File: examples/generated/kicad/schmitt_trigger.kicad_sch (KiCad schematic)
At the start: 6 parts

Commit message: Attempt to create legible symbols.
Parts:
- R1, R2, R3: symbol examples:R -> R
- VCC, VIN: symbol examples:VSOURCE -> VSOURCE
- XU1: symbol examples:OPAMP -> OPAMP
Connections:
- net GND: now also R1.1, VCC.1 (E1), VCC.2 (E2), VIN.2 (E2)
- new net: R3.1, VIN.1 (E1)
- new net: R3.2, XU1.1 (+)
- new net: R1.2, R2.1, XU1.3
- new net: R2.2, XU1.2 (-)
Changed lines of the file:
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@@
     (comment 1 "Generated by mixedsig2cad")
   )
-  (symbol (lib_id "examples:VSOURCE") (at 45.00 40.00 0) (unit 1)
+  (symbol (lib_id "VSOURCE") (at 45.00 40.00 0) (unit 1)
     (in_bom yes) (on_board yes)
     (property "Reference" "VCC" (at 45.0 36.19 0)
@@
     )
   )
-  (symbol (lib_id "examples:VSOURCE") (at 45.00 105.00 90) (unit 1)
+  (symbol (lib_id "VSOURCE") (at 45.00 105.00 90) (unit 1)
     (in_bom yes) (on_board yes)
     (property "Reference" "VIN" (at 45.0 101.19 0)
@@
     )
   )
-  (symbol (lib_id "examples:R") (at 95.00 40.00 90) (unit 1)
+  (symbol (lib_id "R") (at 95.00 40.00 90) (unit 1)
     (in_bom yes) (on_board yes)
     (property "Reference" "R1" (at 95.0 36.19 0)
@@
     )
   )
-  (symbol (lib_id "examples:R") (at 140.00 55.00 90) (unit 1)
+  (symbol (lib_id "R") (at 140.00 55.00 90) (unit 1)
     (in_bom yes) (on_board yes)
     (property "Reference" "R2" (at 140.0 51.19 0)
@@
     )
   )
-  (symbol (lib_id "examples:R") (at 95.00 105.00 90) (unit 1)
+  (symbol (lib_id "R") (at 95.00 105.00 90) (unit 1)
     (in_bom yes) (on_board yes)
     (property "Reference" "R3" (at 95.0 101.19 0)
@@
     )
   )
-  (symbol (lib_id "examples:OPAMP") (at 145.00 85.00 0) (unit 1)
+  (symbol (lib_id "OPAMP") (at 145.00 85.00 0) (unit 1)
     (in_bom yes) (on_board yes)
     (property "Reference" "XU1" (at 145.0 81.19 0)
@@
     )
   )
-  (symbol (lib_id "examples:GND") (at 33.00 26.38 0) (unit 1)
+  (symbol (lib_id "GND") (at 33.00 26.38 0) (unit 1)
     (in_bom yes) (on_board yes)
     (property "Reference" "#PWR0001" (at 33.0 22.570000000000004 0)
@@
     )
   )
-  (symbol (lib_id "examples:VCC") (at 33.00 34.00 0) (unit 1)
+  (symbol (lib_id "VCC") (at 33.00 34.00 0) (unit 1)
     (in_bom yes) (on_board yes)
     (property "Reference" "#PWR0002" (at 33.0 30.19 0)

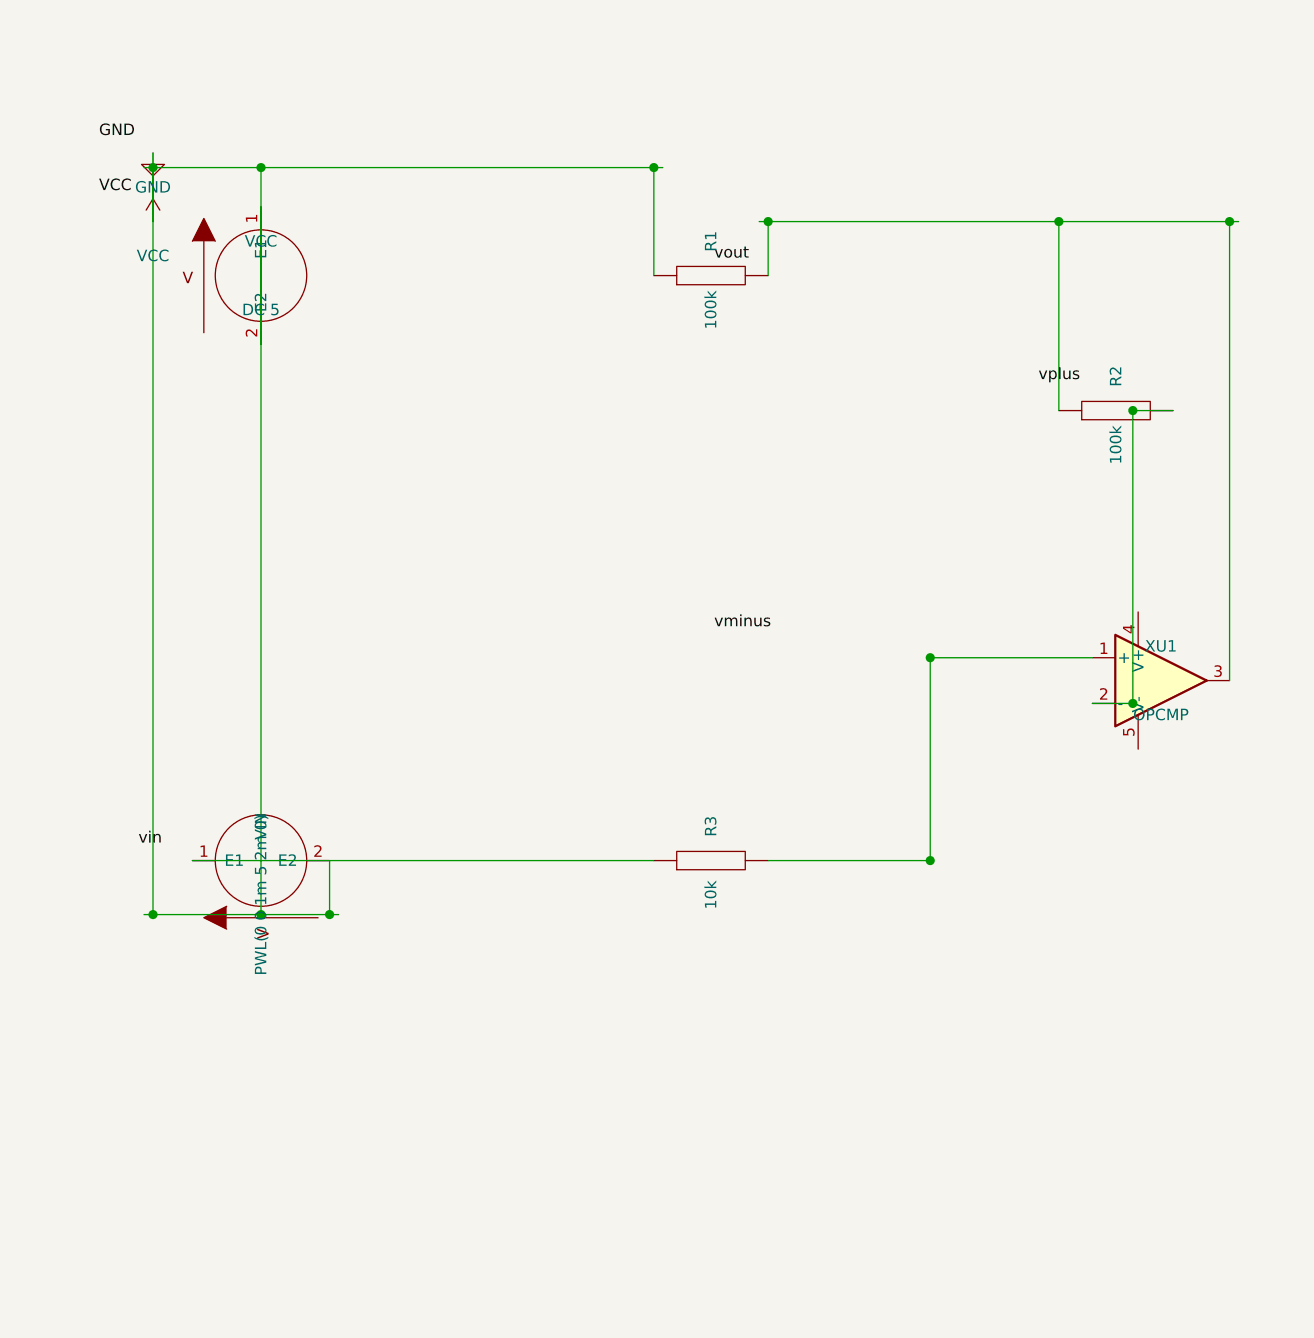
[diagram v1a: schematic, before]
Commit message: Attempt full seperation of circuit concerns into layers.
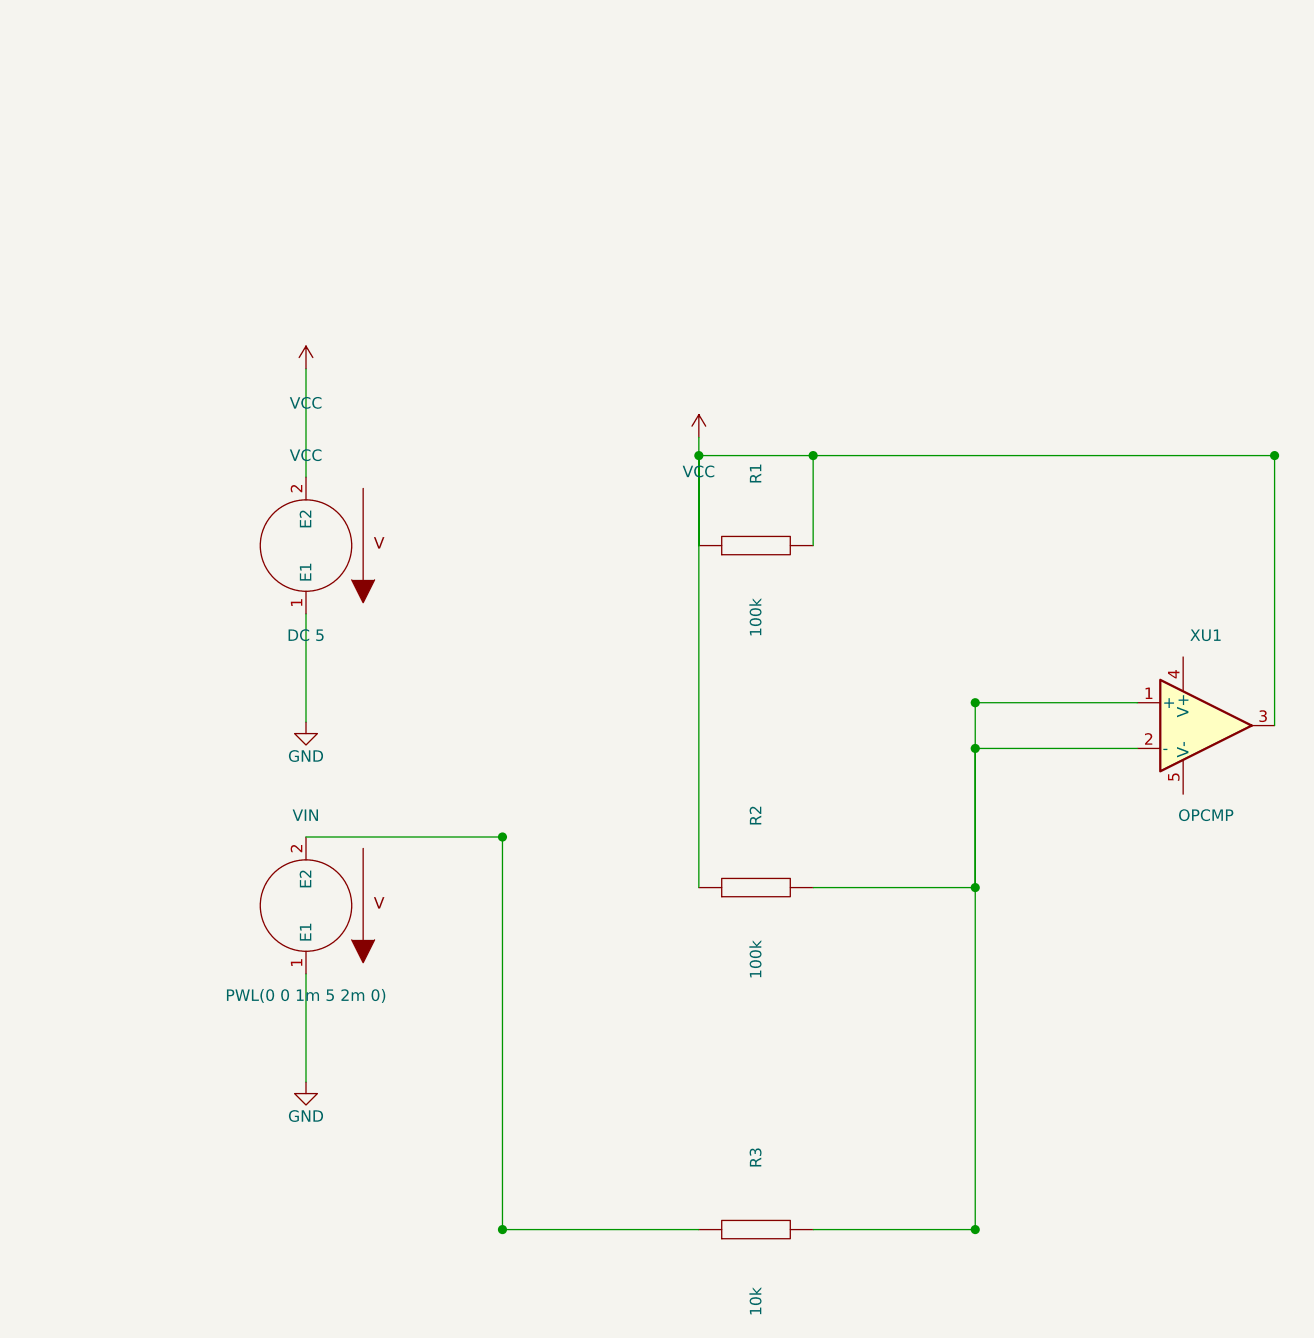
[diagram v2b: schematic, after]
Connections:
- net GND: now also VIN.1 (E1); no longer R1.1, VCC.2 (E2), VIN.2 (E2)
- net at R3.1: now also VIN.2 (E2); no longer VIN.1 (E1)
- net at R3.2, XU1.1 (+): now also R2.2, XU1.2 (-)
- net VCC: now reaches R1.2, R2.1, XU1.3
- net VCC: now also R1.1, VCC.2 (E2)
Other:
- moved on the sheet: R1, R2, R3, VCC, VIN, XU1

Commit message: Add checks for connectivity.
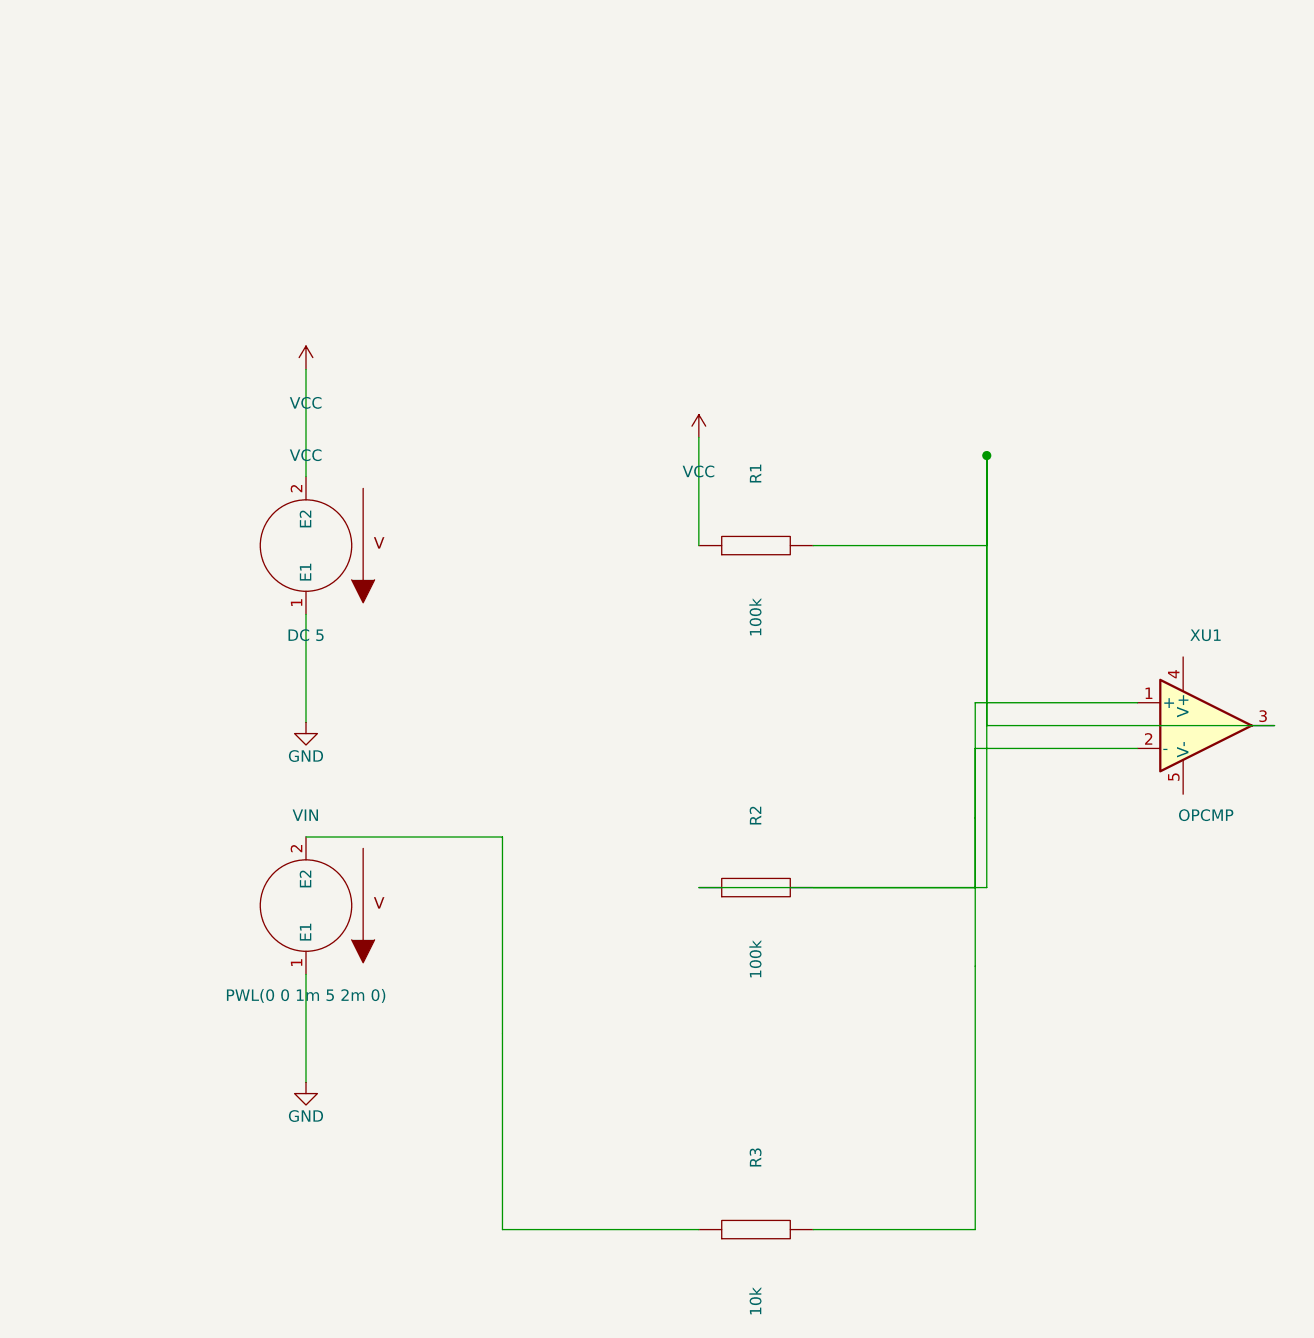
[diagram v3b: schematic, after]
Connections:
- net VCC: no longer R1.2, R2.1, XU1.3
- net at R2.2, R3.2, XU1.1 (+)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: now also R1.2, R2.1, XU1.3
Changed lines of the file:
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@@
     (stroke (width 0) (type solid) (color 0 0 0 0))
   )
-  (wire (pts (xy 71.83 102.38) (xy 71.83 146.00))
+  (wire (pts (xy 71.83 102.38) (xy 71.83 124.19))
     (stroke (width 0) (type solid) (color 0 0 0 0))
   )
-  (wire (pts (xy 71.83 146.00) (xy 93.65 146.00))
+  (wire (pts (xy 93.65 146.00) (xy 71.83 146.00))
+    (stroke (width 0) (type solid) (color 0 0 0 0))
+  )
+  (wire (pts (xy 71.83 146.00) (xy 71.83 124.19))
     (stroke (width 0) (type solid) (color 0 0 0 0))
   )
@@
     (stroke (width 0) (type solid) (color 0 0 0 0))
   )
-  (wire (pts (xy 124.36 146.00) (xy 124.36 87.46))
+  (wire (pts (xy 124.36 146.00) (xy 124.36 116.73))
     (stroke (width 0) (type solid) (color 0 0 0 0))
   )
-  (wire (pts (xy 124.36 87.46) (xy 142.38 87.46))
+  (wire (pts (xy 142.38 87.46) (xy 124.36 87.46))
     (stroke (width 0) (type solid) (color 0 0 0 0))
   )
-  (wire (pts (xy 93.65 60.00) (xy 157.62 60.00))
+  (wire (pts (xy 124.36 87.46) (xy 124.36 116.73))
     (stroke (width 0) (type solid) (color 0 0 0 0))
   )
-  (wire (pts (xy 106.35 70.00) (xy 106.35 60.00))
+  (wire (pts (xy 106.35 70.00) (xy 125.64 70.00))
     (stroke (width 0) (type solid) (color 0 0 0 0))
   )
-  (wire (pts (xy 93.65 108.00) (xy 93.65 60.00))
+  (wire (pts (xy 125.64 70.00) (xy 125.64 60.00))
     (stroke (width 0) (type solid) (color 0 0 0 0))
   )
-  (wire (pts (xy 157.62 90.00) (xy 157.62 60.00))
+  (wire (pts (xy 93.65 108.00) (xy 125.64 108.00))
+    (stroke (width 0) (type solid) (color 0 0 0 0))
+  )
+  (wire (pts (xy 125.64 108.00) (xy 125.64 60.00))
+    (stroke (width 0) (type solid) (color 0 0 0 0))
+  )
+  (wire (pts (xy 157.62 90.00) (xy 125.64 90.00))
+    (stroke (width 0) (type solid) (color 0 0 0 0))
+  )
+  (wire (pts (xy 125.64 90.00) (xy 125.64 60.00))
     (stroke (width 0) (type solid) (color 0 0 0 0))
   )
@@
     (stroke (width 0) (type solid) (color 0 0 0 0))
   )
-  (wire (pts (xy 124.36 108.00) (xy 124.36 92.54))
+  (wire (pts (xy 124.36 108.00) (xy 124.36 100.27))
     (stroke (width 0) (type solid) (color 0 0 0 0))
   )
-  (wire (pts (xy 124.36 92.54) (xy 142.38 92.54))
+  (wire (pts (xy 142.38 92.54) (xy 124.36 92.54))
     (stroke (width 0) (type solid) (color 0 0 0 0))
   )
-  (junction (at 71.83 102.38) (diameter 1.016) (color 0 0 0 0))
-  (junction (at 71.83 146.00) (diameter 1.016) (color 0 0 0 0))
-  (junction (at 124.36 146.00) (diameter 1.016) (color 0 0 0 0))
-  (junction (at 124.36 87.46) (diameter 1.016) (color 0 0 0 0))
-  (junction (at 106.35 60.00) (diameter 1.016) (color 0 0 0 0))
-  (junction (at 93.65 60.00) (diameter 1.016) (color 0 0 0 0))
-  (junction (at 157.62 60.00) (diameter 1.016) (color 0 0 0 0))
-  (junction (at 124.36 108.00) (diameter 1.016) (color 0 0 0 0))
-  (junction (at 124.36 92.54) (diameter 1.016) (color 0 0 0 0))
+  (wire (pts (xy 124.36 92.54) (xy 124.36 100.27))
+    (stroke (width 0) (type solid) (color 0 0 0 0))
+  )
+  (junction (at 125.64 60.00) (diameter 1.016) (color 0 0 0 0))
   (sheet_instances
     (path "/" (page "1"))

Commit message: Attempt to correct strange wiring.
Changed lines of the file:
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@@
     (stroke (width 0) (type solid) (color 0 0 0 0))
   )
-  (wire (pts (xy 50.00 102.38) (xy 71.83 102.38))
+  (wire (pts (xy 50.00 102.38) (xy 50.00 100.50))
     (stroke (width 0) (type solid) (color 0 0 0 0))
   )
-  (wire (pts (xy 71.83 102.38) (xy 71.83 124.19))
+  (wire (pts (xy 50.00 100.50) (xy 91.50 100.50))
     (stroke (width 0) (type solid) (color 0 0 0 0))
   )
-  (wire (pts (xy 93.65 146.00) (xy 71.83 146.00))
+  (wire (pts (xy 91.50 100.50) (xy 91.50 146.00))
     (stroke (width 0) (type solid) (color 0 0 0 0))
   )
-  (wire (pts (xy 71.83 146.00) (xy 71.83 124.19))
+  (wire (pts (xy 91.50 146.00) (xy 93.65 146.00))
     (stroke (width 0) (type solid) (color 0 0 0 0))
   )
-  (wire (pts (xy 106.35 146.00) (xy 124.36 146.00))
+  (wire (pts (xy 106.35 146.00) (xy 140.00 146.00))
     (stroke (width 0) (type solid) (color 0 0 0 0))
   )
-  (wire (pts (xy 124.36 146.00) (xy 124.36 116.73))
+  (wire (pts (xy 140.00 146.00) (xy 140.00 87.46))
     (stroke (width 0) (type solid) (color 0 0 0 0))
   )
-  (wire (pts (xy 142.38 87.46) (xy 124.36 87.46))
+  (wire (pts (xy 140.00 87.46) (xy 142.38 87.46))
     (stroke (width 0) (type solid) (color 0 0 0 0))
   )
-  (wire (pts (xy 124.36 87.46) (xy 124.36 116.73))
+  (wire (pts (xy 106.35 70.00) (xy 124.25 70.00))
     (stroke (width 0) (type solid) (color 0 0 0 0))
   )
-  (wire (pts (xy 106.35 70.00) (xy 125.64 70.00))
+  (wire (pts (xy 124.25 70.00) (xy 124.25 89.00))
     (stroke (width 0) (type solid) (color 0 0 0 0))
   )
-  (wire (pts (xy 125.64 70.00) (xy 125.64 60.00))
+  (wire (pts (xy 93.65 108.00) (xy 124.25 108.00))
     (stroke (width 0) (type solid) (color 0 0 0 0))
   )
-  (wire (pts (xy 93.65 108.00) (xy 125.64 108.00))
+  (wire (pts (xy 124.25 108.00) (xy 124.25 89.00))
     (stroke (width 0) (type solid) (color 0 0 0 0))
   )
-  (wire (pts (xy 125.64 108.00) (xy 125.64 60.00))
+  (wire (pts (xy 157.62 90.00) (xy 124.25 90.00))
     (stroke (width 0) (type solid) (color 0 0 0 0))
   )
-  (wire (pts (xy 157.62 90.00) (xy 125.64 90.00))
+  (wire (pts (xy 124.25 90.00) (xy 124.25 89.00))
     (stroke (width 0) (type solid) (color 0 0 0 0))
   )
-  (wire (pts (xy 125.64 90.00) (xy 125.64 60.00))
+  (wire (pts (xy 106.35 108.00) (xy 140.00 108.00))
     (stroke (width 0) (type solid) (color 0 0 0 0))
   )
-  (wire (pts (xy 106.35 108.00) (xy 124.36 108.00))
+  (wire (pts (xy 140.00 108.00) (xy 140.00 92.54))
     (stroke (width 0) (type solid) (color 0 0 0 0))
   )
-  (wire (pts (xy 124.36 108.00) (xy 124.36 100.27))
+  (wire (pts (xy 140.00 92.54) (xy 142.38 92.54))
     (stroke (width 0) (type solid) (color 0 0 0 0))
   )
-  (wire (pts (xy 142.38 92.54) (xy 124.36 92.54))
-    (stroke (width 0) (type solid) (color 0 0 0 0))
-  )
-  (wire (pts (xy 124.36 92.54) (xy 124.36 100.27))
-    (stroke (width 0) (type solid) (color 0 0 0 0))
-  )
-  (junction (at 125.64 60.00) (diameter 1.016) (color 0 0 0 0))
+  (junction (at 124.25 89.00) (diameter 1.016) (color 0 0 0 0))
   (sheet_instances
     (path "/" (page "1"))

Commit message: Attempt shape and wiring fixes again.
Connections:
- net at R3.1, VIN.2 (E2): now also R1.2, R2.1, XU1.3
- net at R2.2, R3.2, XU1.1 (+)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: no longer R1.2, R2.1, XU1.3
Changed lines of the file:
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@@
     )
   )
-  (wire (pts (xy 50.00 62.38) (xy 50.00 50.38))
+  (wire (pts (xy 50.00 62.38) (xy 50.00 60.50))
     (stroke (width 0) (type solid) (color 0 0 0 0))
   )
-  (wire (pts (xy 50.00 77.62) (xy 50.00 89.62))
+  (wire (pts (xy 50.00 60.50) (xy 56.00 60.50))
     (stroke (width 0) (type solid) (color 0 0 0 0))
   )
-  (wire (pts (xy 50.00 117.62) (xy 50.00 129.62))
+  (wire (pts (xy 56.00 60.50) (xy 56.00 50.38))
     (stroke (width 0) (type solid) (color 0 0 0 0))
   )
-  (wire (pts (xy 93.65 70.00) (xy 93.65 58.00))
+  (wire (pts (xy 56.00 50.38) (xy 50.00 50.38))
+    (stroke (width 0) (type solid) (color 0 0 0 0))
+  )
+  (wire (pts (xy 50.00 77.62) (xy 50.00 79.50))
+    (stroke (width 0) (type solid) (color 0 0 0 0))
+  )
+  (wire (pts (xy 50.00 79.50) (xy 56.00 79.50))
+    (stroke (width 0) (type solid) (color 0 0 0 0))
+  )
+  (wire (pts (xy 56.00 79.50) (xy 56.00 89.62))
+    (stroke (width 0) (type solid) (color 0 0 0 0))
+  )
+  (wire (pts (xy 56.00 89.62) (xy 50.00 89.62))
+    (stroke (width 0) (type solid) (color 0 0 0 0))
+  )
+  (wire (pts (xy 50.00 117.62) (xy 50.00 119.50))
+    (stroke (width 0) (type solid) (color 0 0 0 0))
+  )
+  (wire (pts (xy 50.00 119.50) (xy 56.00 119.50))
+    (stroke (width 0) (type solid) (color 0 0 0 0))
+  )
+  (wire (pts (xy 56.00 119.50) (xy 56.00 129.62))
+    (stroke (width 0) (type solid) (color 0 0 0 0))
+  )
+  (wire (pts (xy 56.00 129.62) (xy 50.00 129.62))
+    (stroke (width 0) (type solid) (color 0 0 0 0))
+  )
+  (wire (pts (xy 93.65 70.00) (xy 91.50 70.00))
+    (stroke (width 0) (type solid) (color 0 0 0 0))
+  )
+  (wire (pts (xy 91.50 70.00) (xy 91.50 65.00))
+    (stroke (width 0) (type solid) (color 0 0 0 0))
+  )
+  (wire (pts (xy 91.50 65.00) (xy 99.65 65.00))
+    (stroke (width 0) (type solid) (color 0 0 0 0))
+  )
+  (wire (pts (xy 99.65 65.00) (xy 99.65 58.00))
+    (stroke (width 0) (type solid) (color 0 0 0 0))
+  )
+  (wire (pts (xy 99.65 58.00) (xy 93.65 58.00))
     (stroke (width 0) (type solid) (color 0 0 0 0))
   )
@@
     (stroke (width 0) (type solid) (color 0 0 0 0))
   )
-  (wire (pts (xy 93.65 108.00) (xy 124.25 108.00))
+  (wire (pts (xy 93.65 108.00) (xy 91.50 108.00))
     (stroke (width 0) (type solid) (color 0 0 0 0))
   )
-  (wire (pts (xy 124.25 108.00) (xy 124.25 89.00))
+  (wire (pts (xy 91.50 108.00) (xy 91.50 89.00))
     (stroke (width 0) (type solid) (color 0 0 0 0))
   )
-  (wire (pts (xy 157.62 90.00) (xy 124.25 90.00))
+  (wire (pts (xy 91.50 89.00) (xy 124.25 89.00))
     (stroke (width 0) (type solid) (color 0 0 0 0))
   )
-  (wire (pts (xy 124.25 90.00) (xy 124.25 89.00))
+  (wire (pts (xy 157.62 90.00) (xy 160.00 90.00))
     (stroke (width 0) (type solid) (color 0 0 0 0))
   )
+  (wire (pts (xy 160.00 90.00) (xy 160.00 45.38))
+    (stroke (width 0) (type solid) (color 0 0 0 0))
+  )
+  (wire (pts (xy 160.00 45.38) (xy 124.25 45.38))
+    (stroke (width 0) (type solid) (color 0 0 0 0))
+  )
+  (wire (pts (xy 124.25 45.38) (xy 124.25 89.00))
+    (stroke (width 0) (type solid) (color 0 0 0 0))
+  )
